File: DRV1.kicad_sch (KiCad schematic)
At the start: 15 parts

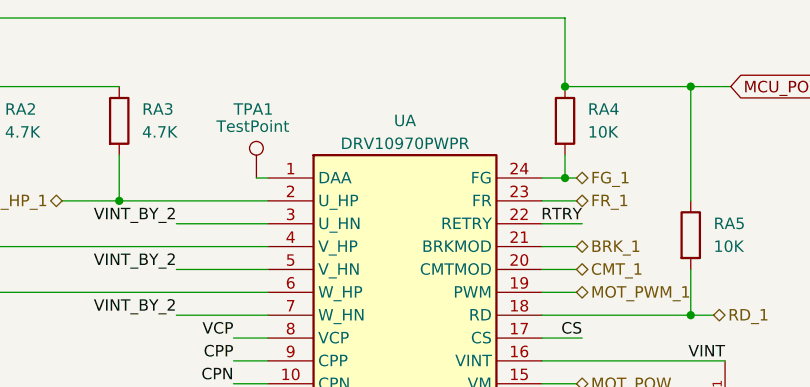
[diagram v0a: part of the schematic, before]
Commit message: Motor symbol corrected, Oscillator circuitry added and external footprints added
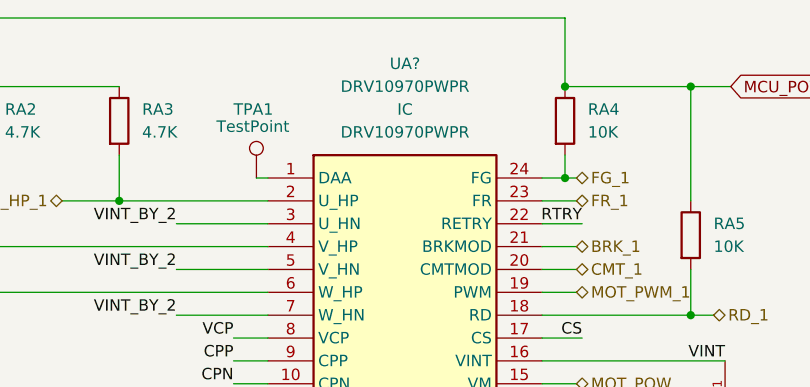
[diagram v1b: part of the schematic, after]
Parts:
- removed UA: DRV10970PWPR, symbol DRV10970PWPR:DRV10970PWPR
- added UA?: DRV10970PWPR, DRV10970PWPR:SOP65P640X120-25N, symbol DRV10970PWPR:DRV10970PWPR
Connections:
- net BRK_1: now also UA?.21 (BRKMOD)
- net CMT_1: now also UA?.20 (CMTMOD)
- net CPN: now also UA?.10 (CPN)
- net CPP: now also UA?.9 (CPP)
- net CS: now also UA?.17 (CS)
- net FG_1: now also UA?.24 (FG)
- net FR_1: now also UA?.23 (FR)
- net GND: now also UA?.12 (GND), UA?.25 (EP)
- net MOT_POW: now also UA?.15 (VM)
- net MOT_PWM_1: now also UA?.19 (PWM)
- net RD_1: now also UA?.18 (RD)
- net RTRY: now also UA?.22 (RETRY)
- net U_1: now also UA?.14 (U)
- net U_HP_1: now also UA?.2 (U_HP)
- net VCP: now also UA?.8 (VCP)
- net VINT: now also UA?.16 (VINT)
- net VINT_BY_2: now also UA?.3 (U_HN), UA?.5 (V_HN), UA?.7 (W_HN)
- net V_1: now also UA?.13 (V)
- net V_HP_1: now also UA?.4 (V_HP)
- net W_1: now also UA?.11 (W)
- net W_HP_1: now also UA?.6 (W_HP)
- net at TPA1.1: now also UA?.1 (DAA)
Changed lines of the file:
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@@
   (symbol (lib_id "power:GND") (at 154.94 154.305 0) (unit 1)
     (in_bom yes) (on_board yes) (fields_autoplaced)
-    (property "Reference" "#PWR?" (id 0) (at 154.94 160.655 0)
+    (property "Reference" "#PWR0111" (id 0) (at 154.94 160.655 0)
       (effects (font (size 1.27 1.27)) hide)
     )
@@
   (symbol (lib_id "power:GND") (at 205.74 111.76 0) (unit 1)
     (in_bom yes) (on_board yes) (fields_autoplaced)
-    (property "Reference" "#PWR?" (id 0) (at 205.74 118.11 0)
+    (property "Reference" "#PWR0114" (id 0) (at 205.74 118.11 0)
       (effects (font (size 1.27 1.27)) hide)
     )
@@
   (symbol (lib_id "power:GND") (at 222.25 149.86 0) (unit 1)
     (in_bom yes) (on_board yes) (fields_autoplaced)
-    (property "Reference" "#PWR?" (id 0) (at 222.25 156.21 0)
+    (property "Reference" "#PWR0112" (id 0) (at 222.25 156.21 0)
       (effects (font (size 1.27 1.27)) hide)
     )
@@
   (symbol (lib_id "power:GND") (at 138.43 114.3 0) (unit 1)
     (in_bom yes) (on_board yes) (fields_autoplaced)
-    (property "Reference" "#PWR?" (id 0) (at 138.43 120.65 0)
+    (property "Reference" "#PWR0109" (id 0) (at 138.43 120.65 0)
       (effects (font (size 1.27 1.27)) hide)
     )
@@
   (symbol (lib_id "power:GND") (at 189.23 119.38 0) (unit 1)
     (in_bom yes) (on_board yes) (fields_autoplaced)
-    (property "Reference" "#PWR?" (id 0) (at 189.23 125.73 0)
+    (property "Reference" "#PWR0113" (id 0) (at 189.23 125.73 0)
       (effects (font (size 1.27 1.27)) hide)
     )
@@
   (symbol (lib_id "power:GND") (at 153.67 127 0) (unit 1)
     (in_bom yes) (on_board yes) (fields_autoplaced)
-    (property "Reference" "#PWR?" (id 0) (at 153.67 133.35 0)
+    (property "Reference" "#PWR0110" (id 0) (at 153.67 133.35 0)
       (effects (font (size 1.27 1.27)) hide)
     )
@@
     (pin "1")
   )
-  (symbol (lib_id "Device:R") (at 213.36 135.89 90) (unit 1)
-    (in_bom yes) (on_board yes) (fields_autoplaced)
-    (property "Reference" "RA8" (id 0) (at 213.36 129.54 90))
-    (property "Value" "0" (id 1) (at 213.36 132.08 90))
-    (property "Footprint" "" (id 2) (at 213.36 137.668 90)
-      (effects (font (size 1.27 1.27)) hide)
-    )
-    (property "Datasheet" "~" (id 3) (at 213.36 135.89 0)
-      (effects (font (size 1.27 1.27)) hide)
-    )
-    (pin "1")
-    (pin "2")
-  )
-  (symbol (lib_id "Device:R") (at 121.92 80.01 0) (unit 1)
-    (in_bom yes) (on_board yes) (fields_autoplaced)
-    (property "Reference" "RA3" (id 0) (at 124.46 78.7399 0)
-      (effects (font (size 1.27 1.27)) (justify left))
-    )
-    (property "Value" "4.7K" (id 1) (at 124.46 81.2799 0)
-      (effects (font (size 1.27 1.27)) (justify left))
-    )
-    (property "Footprint" "" (id 2) (at 120.142 80.01 90)
-      (effects (font (size 1.27 1.27)) hide)
-    )
-    (property "Datasheet" "~" (id 3) (at 121.92 80.01 0)
-      (effects (font (size 1.27 1.27)) hide)
-    )
-    (pin "1")
-    (pin "2")
-  )
-  (symbol (lib_id "Device:R") (at 185.42 92.71 0) (unit 1)
-    (in_bom yes) (on_board yes) (fields_autoplaced)
-    (property "Reference" "RA5" (id 0) (at 187.96 91.4399 0)
-      (effects (font (size 1.27 1.27)) (justify left))
-    )
-    (property "Value" "10K" (id 1) (at 187.96 93.9799 0)
-      (effects (font (size 1.27 1.27)) (justify left))
-    )
-    (property "Footprint" "" (id 2) (at 183.642 92.71 90)
-      (effects (font (size 1.27 1.27)) hide)
-    )
-    (property "Datasheet" "~" (id 3) (at 185.42 92.71 0)
-      (effects (font (size 1.27 1.27)) hide)
-    )
-    (pin "1")
-    (pin "2")
-  )
   (symbol (lib_id "DRV10970PWPR:DRV10970PWPR") (at 138.43 86.36 0) (unit 1)
-    (in_bom yes) (on_board yes)
-    (property "Reference" "UA" (id 0) (at 153.67 80.01 0))
-    (property "Value" "DRV10970PWPR" (id 1) (at 153.67 82.55 0))
-    (property "Footprint" "" (id 2) (at 138.43 86.36 0)
+    (in_bom yes) (on_board yes) (fields_autoplaced)
+    (property "Reference" "UA?" (id 0) (at 153.67 73.66 0))
+    (property "Value" "DRV10970PWPR" (id 1) (at 153.67 76.2 0))
+    (property "Footprint" "DRV10970PWPR:SOP65P640X120-25N" (id 2) (at 138.43 86.36 0)
       (effects (font (size 1.27 1.27)) hide)
     )
@@
       (effects (font (size 1.27 1.27)) hide)
     )
-    (property "Reference_1" "IC" (id 4) (at 153.67 78.74 0)
-      (effects (font (size 1.27 1.27)) hide)
-    )
-    (property "Value_1" "DRV10970PWPR" (id 5) (at 153.67 81.28 0)
-      (effects (font (size 1.27 1.27)) hide)
-    )
+    (property "Reference_1" "IC" (id 4) (at 153.67 78.74 0))
+    (property "Value_1" "DRV10970PWPR" (id 5) (at 153.67 81.28 0))
     (property "Footprint_1" "SOP65P640X120-25N" (id 6) (at 165.1 181.28 0)
       (effects (font (size 1.27 1.27)) (justify left top) hide)
@@
     (pin "9")
   )
+  (symbol (lib_id "Device:R") (at 213.36 135.89 90) (unit 1)
+    (in_bom yes) (on_board yes) (fields_autoplaced)
+    (property "Reference" "RA8" (id 0) (at 213.36 129.54 90))
+    (property "Value" "0" (id 1) (at 213.36 132.08 90))
+    (property "Footprint" "" (id 2) (at 213.36 137.668 90)
+      (effects (font (size 1.27 1.27)) hide)
+    )
+    (property "Datasheet" "~" (id 3) (at 213.36 135.89 0)
+      (effects (font (size 1.27 1.27)) hide)
+    )
+    (pin "1")
+    (pin "2")
+  )
+  (symbol (lib_id "Device:R") (at 121.92 80.01 0) (unit 1)
+    (in_bom yes) (on_board yes) (fields_autoplaced)
+    (property "Reference" "RA3" (id 0) (at 124.46 78.7399 0)
+      (effects (font (size 1.27 1.27)) (justify left))
+    )
+    (property "Value" "4.7K" (id 1) (at 124.46 81.2799 0)
+      (effects (font (size 1.27 1.27)) (justify left))
+    )
+    (property "Footprint" "" (id 2) (at 120.142 80.01 90)
+      (effects (font (size 1.27 1.27)) hide)
+    )
+    (property "Datasheet" "~" (id 3) (at 121.92 80.01 0)
+      (effects (font (size 1.27 1.27)) hide)
+    )
+    (pin "1")
+    (pin "2")
+  )
+  (symbol (lib_id "Device:R") (at 185.42 92.71 0) (unit 1)
+    (in_bom yes) (on_board yes) (fields_autoplaced)
+    (property "Reference" "RA5" (id 0) (at 187.96 91.4399 0)
+      (effects (font (size 1.27 1.27)) (justify left))
+    )
+    (property "Value" "10K" (id 1) (at 187.96 93.9799 0)
+      (effects (font (size 1.27 1.27)) (justify left))
+    )
+    (property "Footprint" "" (id 2) (at 183.642 92.71 90)
+      (effects (font (size 1.27 1.27)) hide)
+    )
+    (property "Datasheet" "~" (id 3) (at 185.42 92.71 0)
+      (effects (font (size 1.27 1.27)) hide)
+    )
+    (pin "1")
+    (pin "2")
+  )
   (symbol (lib_id "pspice:C") (at 189.23 113.03 0) (unit 1)

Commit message: MCU interfaces are done! Check the Changes and Complete ERC modifications
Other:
- company: (none) -> Parikshit Student Satellite Team
- title: (none) -> AOCS BOARD
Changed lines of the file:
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@@
 (kicad_sch (version 20211123) (generator eeschema)
   (paper "A4")
+  (title_block
+    (title "AOCS BOARD")
+    (company "Parikshit Student Satellite Team")
+  )
   (junction (at 185.42 101.6) (diameter 0) (color 0 0 0 0)
   )
@@
   )
   (wire (pts (xy 168.91 96.52) (xy 172.72 96.52))
+    (stroke (width 0) (type default) (color 0 0 0 0))
+  )
+  (wire (pts (xy 27.94 121.285) (xy 27.94 120.015))
     (stroke (width 0) (type default) (color 0 0 0 0))
   )
@@
     (pin "1")
     (pin "2")
+  )
+  (symbol (lib_id "power:GND") (at 27.94 121.285 0) (unit 1)
+    (in_bom yes) (on_board yes) (fields_autoplaced)
+    (property "Reference" "#PWR0267" (id 0) (at 27.94 127.635 0)
+      (effects (font (size 1.27 1.27)) hide)
+    )
+    (property "Value" "GND" (id 1) (at 27.94 125.73 0))
+    (property "Footprint" "" (id 2) (at 27.94 121.285 0)
+      (effects (font (size 1.27 1.27)) hide)
+    )
+    (property "Datasheet" "" (id 3) (at 27.94 121.285 0)
+      (effects (font (size 1.27 1.27)) hide)
+    )
+    (pin "1")
   )
   (symbol (lib_id "power:GND") (at 138.43 114.3 0) (unit 1)
@@
     (pin "2")
   )
+  (symbol (lib_id "power:PWR_FLAG") (at 27.94 120.015 0) (unit 1)
+    (in_bom yes) (on_board yes) (fields_autoplaced)
+    (property "Reference" "#FLG0103" (id 0) (at 27.94 118.11 0)
+      (effects (font (size 1.27 1.27)) hide)
+    )
+    (property "Value" "PWR_FLAG" (id 1) (at 27.94 114.3 0))
+    (property "Footprint" "" (id 2) (at 27.94 120.015 0)
+      (effects (font (size 1.27 1.27)) hide)
+    )
+    (property "Datasheet" "~" (id 3) (at 27.94 120.015 0)
+      (effects (font (size 1.27 1.27)) hide)
+    )
+    (pin "1")
+  )
   (symbol (lib_id "Device:R") (at 205.74 107.95 0) (unit 1)
